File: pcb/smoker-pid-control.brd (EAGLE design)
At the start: 90 x 60 mm, 12 parts, among them SW1 EC12E_SW

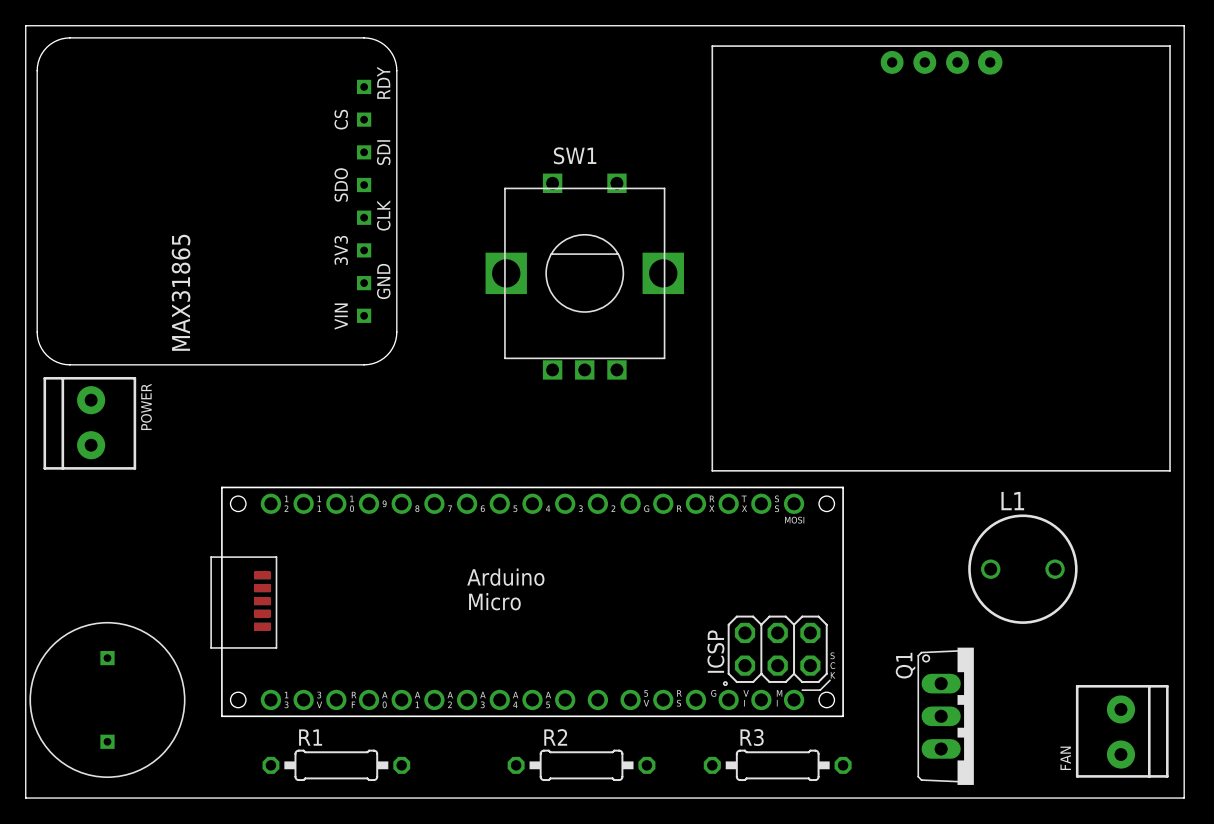
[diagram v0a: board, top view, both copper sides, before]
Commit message: pcb with pulldown on gate
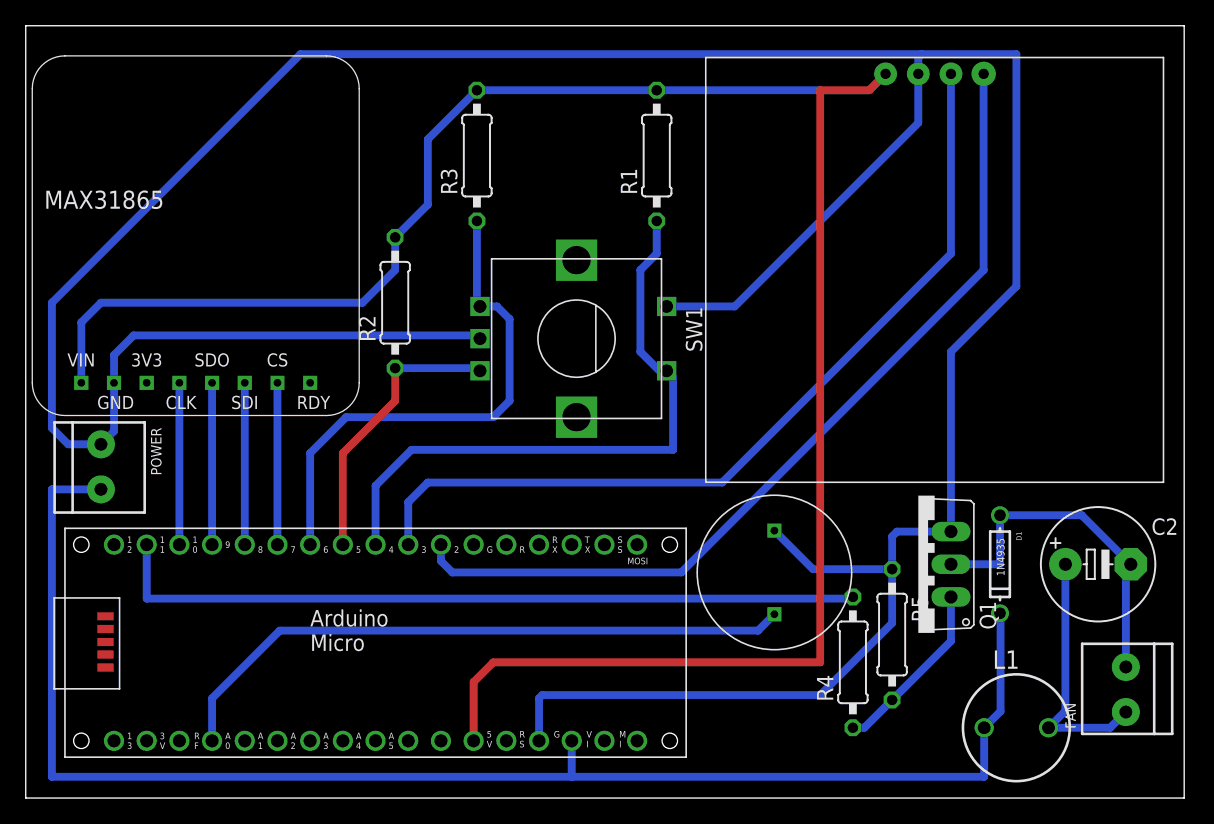
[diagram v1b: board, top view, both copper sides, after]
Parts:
- added C2: 47uF, rcl:E5-8,5
- added D1: 1N4935, adafruit:DO-1N4148
- added R4: 1.2k, rcl:0207/10
- added R5: 100k, rcl:0207/10
- FAN: value (none) -> 12V Fan
- L1: value 07HCP-100U -> 47mH
- POWER: value (none) -> 12V
- Q1: value (none) -> IRLIZ44N
- moved R1 53.5 mm to (49.0, 49.9), turned to 90 degrees
- moved R3 52.8 mm to (35.1, 49.9), turned to 90 degrees
- moved U$3 52.8 mm to (58.2, 17.5)
- moved R2 38.7 mm to (28.7, 38.5), turned to 90 degrees
- moved PCB1 12.6 mm to (3.05, 3.17)
- moved Q1 12.6 mm to (69.3, 18.2), turned to 90 degrees
- moved L1 12.3 mm to (77.0, 5.46)
- moved SW1 5.11 mm to (42.8, 35.7), turned to 270 degrees
- moved POWER 3.51 mm to (5.84, 25.8)
- moved FAN 3.32 mm to (85.5, 8.38)
- moved U$1 3.14 mm to (13.2, 43.7), turned to 0 degrees
- moved U$2 1.02 mm to (66.8, 56.3)
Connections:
- new net N$11: C2.+, FAN.2, L1.2
- new net N$12: Q1.1, R4.1, R5.2
- new net N$14: C2.-, D1.A, FAN.1, Q1.2
- new net PWM: PCB1.D11, R4.2
- net +12V: now also D1.C, L1.1
- net GND: now also Q1.3, R5.1
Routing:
- net GND: track 0.00 -> 258.6 mm
- net +5V: track 0.00 -> 161.8 mm
- net +12V: track 0.00 -> 114.6 mm
- net N$1: track 0.00 -> 68.8 mm
- net N$2: track 0.00 -> 67.4 mm
- net PWM: track 0.00 -> 59.1 mm
- net N$10: track 0.00 -> 49.7 mm
- net N$4: track 0.00 -> 48.7 mm
- net N$9: track 0.00 -> 40.1 mm
- net N$14: track 0.00 -> 27.5 mm
- net N$8: track 0.00 -> 22.1 mm
- net N$11: track 0.00 -> 19.8 mm
- net N$12: track 0.00 -> 13.8 mm
- net N$7: track 0.00 -> 12.6 mm
- net N$6: track 0.00 -> 12.6 mm
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
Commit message: fix drill hole sizes, fix oled wiring bug
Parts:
- R2: device rcl:0207/10 -> rcl:0207/15
- moved R3 0.13 mm to (35.1, 50.0)
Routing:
- net GND: track 258.6 -> 278.1 mm
- net N$9: track 40.1 -> 36.0 mm
- net N$8: track 22.1 -> 20.2 mm
- net PWM: track 59.1 -> 57.6 mm
- net N$4: track 48.7 -> 47.8 mm
- net +5V: track 161.8 -> 162.6 mm

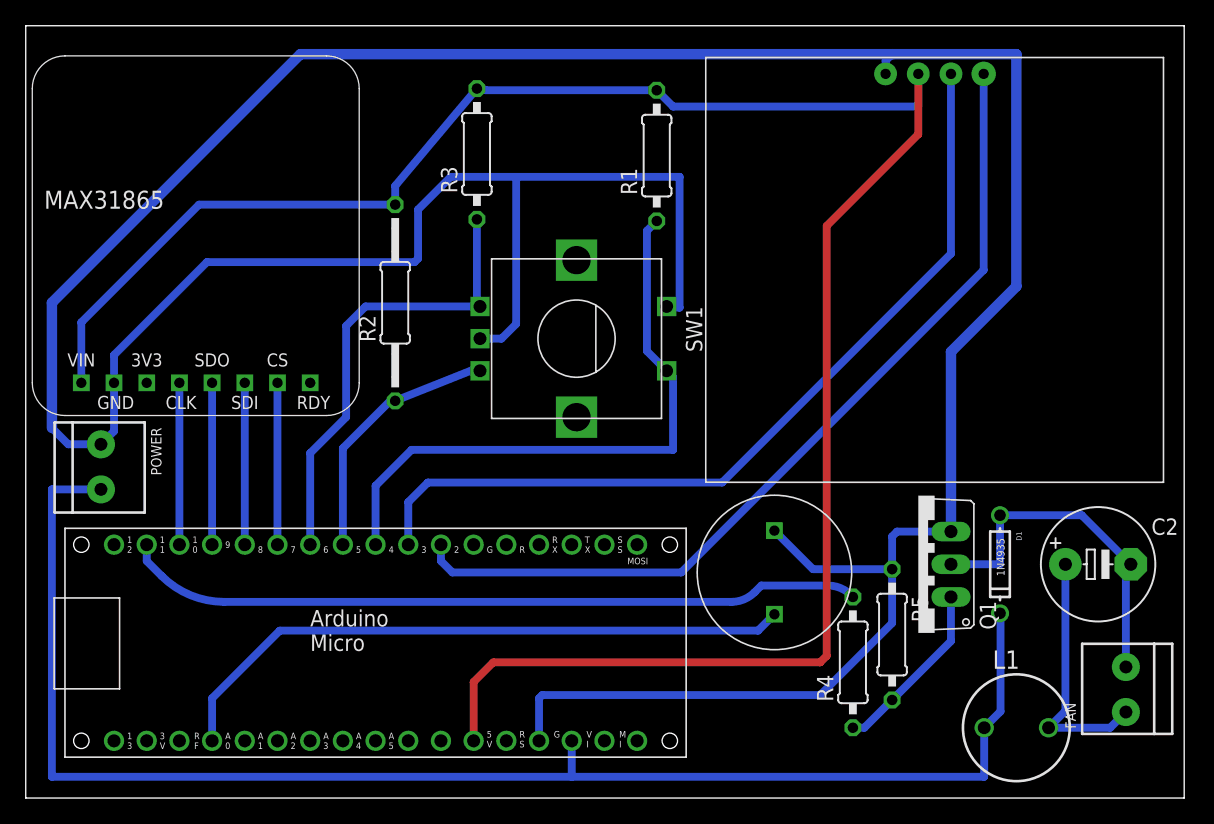
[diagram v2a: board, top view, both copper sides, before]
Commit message: single layer Layout, groundplane fix, stronger airwires
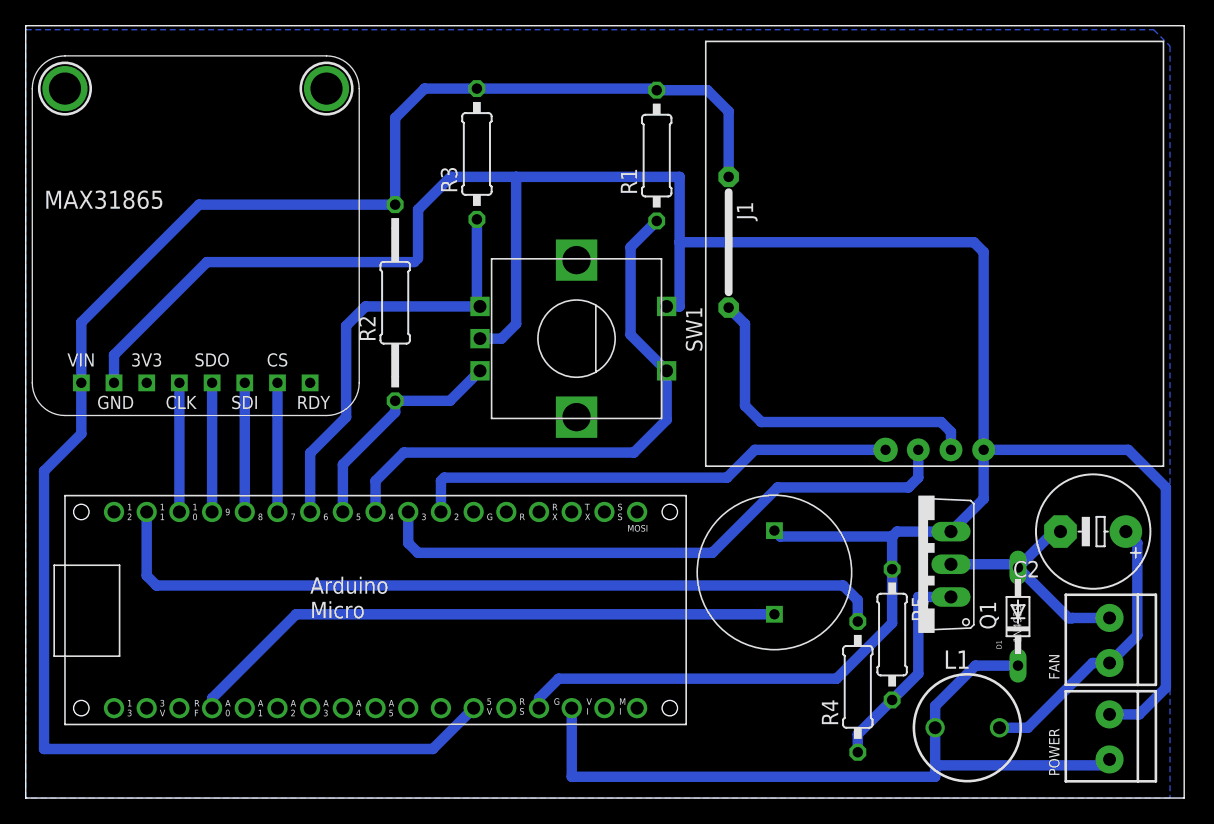
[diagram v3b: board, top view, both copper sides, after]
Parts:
- added J1: J10MM, jumper:10
- D1: device adafruit:DO-1N4148 -> diode:DO34-7
- moved POWER 81.1 mm to (84.2, 4.70), turned to 90 degrees
- moved U$2 30.2 mm to (74.4, 27.1), turned to 180 degrees
- moved D1 4.30 mm to (77.1, 14.1), turned to 90 degrees
- moved FAN 4.02 mm to (84.2, 12.2)
- moved L1 3.81 mm to (73.2, 5.46)
- moved C2 2.57 mm to (82.9, 20.7), turned to 180 degrees
- moved PCB1 2.54 mm to (3.05, 5.71)
- moved R4 1.94 mm to (64.6, 8.64)
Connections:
- new net N$13: J1.2, U$2.VCC
- net +12V: now also POWER.2; no longer POWER.1
- net +5V: now also J1.1; no longer U$2.VCC
- net GND: now also POWER.1; no longer POWER.2
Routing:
- net GND: track 278.1 -> 214.1 mm
- net +12V: track 114.6 -> 60.5 mm
- net N$1: track 68.8 -> 38.0 mm
- net N$13: track 0.00 -> 26.4 mm
- net +5V: track 162.6 -> 136.6 mm
- net N$2: track 67.4 -> 46.9 mm
- net N$14: track 27.5 -> 18.5 mm
- net PWM: track 57.6 -> 62.6 mm
- net N$4: track 47.8 -> 44.4 mm
- net N$12: track 13.8 -> 16.6 mm
- net N$10: track 49.7 -> 47.2 mm
- net N$7: track 12.6 -> 10.0 mm
- net N$6: track 12.6 -> 10.0 mm
- net N$5: track 12.6 -> 10.0 mm
- net N$3: track 12.6 -> 10.0 mm
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- added copper zone on layer 16, net GND

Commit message: final pcb
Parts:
- moved U$2 8.13 mm to (80.8, 32.1)
- moved U$3 8.13 mm to (64.5, 22.6)
- moved POWER 8.13 mm to (90.6, 9.78)
- moved C2 8.13 mm to (89.3, 25.8)
- moved FAN 8.13 mm to (90.6, 17.3)
- moved R3 8.13 mm to (41.4, 55.1)
- moved J1 8.13 mm to (61.0, 48.3)
- moved PCB1 8.13 mm to (9.40, 10.8)
- moved R1 8.13 mm to (55.4, 55.0)
- moved SW1 8.13 mm to (49.1, 40.8)
- moved R2 8.13 mm to (35.1, 43.6)
- moved R5 8.13 mm to (73.7, 17.8)
- moved U$1 8.13 mm to (19.6, 48.8)
- moved D1 8.13 mm to (83.4, 19.2)
- moved L1 8.13 mm to (79.5, 10.5)
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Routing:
- net +5V: track 136.6 -> 132.5 mm
- net GND: track 214.1 -> 216.5 mm
- net +12V: track 60.5 -> 59.1 mm
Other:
- board size 90 x 60 mm -> 100 x 70 mm

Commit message: optimise space
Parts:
- moved SW1 2.54 mm to (46.6, 40.8)
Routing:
- net GND: track 216.5 -> 220.9 mm
- net N$8: track 17.9 -> 15.3 mm
- net N$9: track 33.5 -> 31.8 mm
- net N$4: track 44.4 -> 45.2 mm
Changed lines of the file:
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@@
 <setting verticaltext="up"/>
 </settings>
-<grid distance="50" unitdist="mil" unit="mm" style="lines" multiple="1" display="no" altdistance="5" altunitdist="mil" altunit="mil"/>
+<grid distance="50" unitdist="mil" unit="mil" style="lines" multiple="1" display="no" altdistance="5" altunitdist="mil" altunit="mil"/>
 <layers>
 <layer number="1" name="Top" color="4" fill="1" visible="yes" active="yes"/>
@@
 <element name="U$1" library="smoker-pid-control" package="MAX31865-BRD" value="ADAFRUIT-MAX31865" x="19.558" y="48.768" smashed="yes" grouprefs="G1"/>
 <element name="U$2" library="smoker-pid-control" package="1.3&quot;OLED" value="13&quot;OLED13&quot;OLED" x="80.772" y="32.131" smashed="yes" rot="R180" grouprefs="G1"/>
-<element name="SW1" library="smoker-pid-control" package="ALPS_EC12E_SW" package3d_urn="urn:adsk.eagle:package:27083/1" value="EC12E_SW" x="49.142" y="40.771" smashed="yes" rot="R270" grouprefs="G1">
-<attribute name="MF" value="" x="49.142" y="40.771" size="1.778" layer="27" rot="R270" display="off"/>
-<attribute name="MPN" value="EC12E2424407" x="49.142" y="40.771" size="1.778" layer="27" rot="R270" display="off"/>
-<attribute name="NAME" x="57.642" y="43.271" size="1.27" layer="25" rot="R270"/>
-<attribute name="OC_FARNELL" value="1520813" x="49.142" y="40.771" size="1.778" layer="27" rot="R270" display="off"/>
-<attribute name="OC_NEWARK" value="74M1068" x="49.142" y="40.771" size="1.778" layer="27" rot="R270" display="off"/>
-<attribute name="POPULARITY" value="3" x="49.142" y="40.771" size="1.778" layer="27" rot="R270" display="off"/>
-<attribute name="VALUE" x="40.142" y="37.271" size="1.27" layer="27" rot="R90"/>
+<element name="SW1" library="smoker-pid-control" package="ALPS_EC12E_SW" package3d_urn="urn:adsk.eagle:package:27083/1" value="EC12E_SW" x="46.602" y="40.771" smashed="yes" rot="R270" grouprefs="G1">
+<attribute name="MF" value="" x="46.602" y="40.771" size="1.778" layer="27" rot="R270" display="off"/>
+<attribute name="MPN" value="EC12E2424407" x="46.602" y="40.771" size="1.778" layer="27" rot="R270" display="off"/>
+<attribute name="NAME" x="55.102" y="43.271" size="1.27" layer="25" rot="R270"/>
+<attribute name="OC_FARNELL" value="1520813" x="46.602" y="40.771" size="1.778" layer="27" rot="R270" display="off"/>
+<attribute name="OC_NEWARK" value="74M1068" x="46.602" y="40.771" size="1.778" layer="27" rot="R270" display="off"/>
+<attribute name="POPULARITY" value="3" x="46.602" y="40.771" size="1.778" layer="27" rot="R270" display="off"/>
+<attribute name="VALUE" x="37.602" y="37.271" size="1.27" layer="27" rot="R90"/>
 </element>
 <element name="POWER" library="smoker-pid-control" package="TERMBLOCK_1X2-3.5MM" value="12V" x="90.551" y="9.779" smashed="yes" rot="R90" grouprefs="G1">
@@
 <wire x1="73.66" y1="22.86" x2="73.66" y2="18.669" width="0.8128" layer="16"/>
 <wire x1="73.66" y1="18.669" x2="69.342" y2="14.351" width="0.8128" layer="16"/>
-<wire x1="41.642" y1="40.771" x2="43.311" y2="40.771" width="0.8128" layer="16"/>
-<wire x1="43.311" y1="40.771" x2="44.45" y2="41.91" width="0.8128" layer="16"/>
-<wire x1="44.45" y1="41.91" x2="44.45" y2="53.34" width="0.8128" layer="16"/>
-<wire x1="44.45" y1="53.34" x2="39.37" y2="53.34" width="0.8128" layer="16"/>
+<wire x1="39.102" y1="40.771" x2="43.18" y2="40.771" width="0.8128" layer="16"/>
+<wire x1="43.18" y1="40.771" x2="43.18" y2="53.34" width="0.8128" layer="16"/>
+<wire x1="43.18" y1="53.34" x2="39.37" y2="53.34" width="0.8128" layer="16"/>
 <wire x1="36.83" y1="50.8" x2="36.83" y2="46.99" width="0.8128" layer="16"/>
 <wire x1="36.83" y1="46.99" x2="36.556715625" y2="46.716715625" width="0.6096" layer="16"/>
 <wire x1="36.556715625" y1="46.716715625" x2="20.427715625" y2="46.716715625" width="0.8128" layer="16"/>
 <wire x1="39.37" y1="53.34" x2="36.83" y2="50.8" width="0.8128" layer="16"/>
-<wire x1="57.15" y1="43.271" x2="56.142" y2="43.271" width="0.8128" layer="16"/>
+<wire x1="57.15" y1="43.271" x2="53.602" y2="43.271" width="0.8128" layer="16"/>
 <wire x1="57.15" y1="48.26" x2="57.15" y2="43.271" width="0.8128" layer="16"/>
 <wire x1="64.516" y1="25.856" x2="64.972" y2="25.4" width="0.8128" layer="16"/>
@@
 </polygon>
 <wire x1="58.42" y1="48.26" x2="57.15" y2="48.26" width="0.8128" layer="16"/>
-<wire x1="44.45" y1="53.34" x2="45.72" y2="54.61" width="0.8128" layer="16"/>
-<wire x1="45.72" y1="54.61" x2="57.15" y2="54.61" width="0.8128" layer="16"/>
+<wire x1="43.18" y1="53.34" x2="44.45" y2="54.61" width="0.8128" layer="16"/>
+<wire x1="44.45" y1="54.61" x2="57.15" y2="54.61" width="0.8128" layer="16"/>
 <wire x1="57.15" y1="54.61" x2="58.42" y2="53.34" width="0.8128" layer="16"/>
 <wire x1="58.42" y1="53.34" x2="58.42" y2="48.26" width="0.8128" layer="16"/>
@@
 <contactref element="SW1" pad="E"/>
 <contactref element="PCB1" pad="D4"/>
-<wire x1="53.34" y1="47.879" x2="55.372" y2="49.911" width="0.8128" layer="16"/>
-<wire x1="53.34" y1="41.073" x2="53.34" y2="47.879" width="0.8128" layer="16"/>
+<wire x1="54.102" y1="49.911" x2="55.372" y2="49.911" width="0.8128" layer="16"/>
+<wire x1="54.102" y1="49.911" x2="50.8" y2="46.609" width="0.8128" layer="16"/>
+<wire x1="50.8" y1="41.073" x2="50.8" y2="46.609" width="0.8128" layer="16"/>
 <wire x1="53.602" y1="31.921" x2="35.731" y2="31.921" width="0.8128" layer="16"/>
-<wire x1="56.142" y1="34.461" x2="53.602" y2="31.921" width="0.8128" layer="16"/>
-<wire x1="56.142" y1="34.461" x2="56.142" y2="38.271" width="0.8128" layer="16"/>
+<wire x1="53.602" y1="31.921" x2="53.602" y2="38.271" width="0.8128" layer="16"/>
 <wire x1="33.528" y1="27.305" x2="33.528" y2="29.718" width="0.8128" layer="16"/>
 <wire x1="35.731" y1="31.921" x2="33.528" y2="29.718" width="0.8128" layer="16"/>
-<wire x1="56.142" y1="38.271" x2="53.34" y2="41.073" width="0.8128" layer="16"/>
+<wire x1="53.602" y1="38.271" x2="50.8" y2="41.073" width="0.8128" layer="16"/>
 </signal>
 <signal name="N$8">
@@
 <wire x1="30.988" y1="30.988" x2="35.052" y2="35.052" width="0.8128" layer="16"/>
 <wire x1="35.052" y1="35.052" x2="35.052" y2="35.941" width="0.8128" layer="16"/>
-<wire x1="35.052" y1="35.941" x2="39.312" y2="35.941" width="0.8128" layer="16"/>
-<wire x1="39.312" y1="35.941" x2="41.642" y2="38.271" width="0.8128" layer="16"/>
+<wire x1="35.052" y1="35.941" x2="36.772" y2="35.941" width="0.8128" layer="16"/>
+<wire x1="36.772" y1="35.941" x2="39.102" y2="38.271" width="0.8128" layer="16"/>
 </signal>
 <signal name="N$9">
@@
 <contactref element="SW1" pad="A"/>
 <contactref element="PCB1" pad="D6"/>
-<wire x1="41.642" y1="43.271" x2="32.752" y2="43.271" width="0.8128" layer="16"/>
+<wire x1="39.102" y1="43.271" x2="32.752" y2="43.271" width="0.8128" layer="16"/>
 <wire x1="32.752" y1="43.271" x2="31.242" y2="41.761" width="0.8128" layer="16"/>
 <wire x1="31.242" y1="34.671" x2="31.242" y2="41.761" width="0.8128" layer="16" grouprefs="G1"/>
 <wire x1="28.448" y1="31.877" x2="28.448" y2="27.305" width="0.8128" layer="16" grouprefs="G1"/>
 <wire x1="31.242" y1="34.671" x2="28.448" y2="31.877" width="0.8128" layer="16" grouprefs="G1"/>
-<wire x1="41.402" y1="50.038" x2="41.402" y2="43.511" width="0.8128" layer="16"/>
-<wire x1="41.402" y1="43.511" x2="41.642" y2="43.271" width="0.6096" layer="16"/>
+<wire x1="41.402" y1="50.038" x2="40.132" y2="48.768" width="0.8128" layer="16"/>
+<wire x1="40.132" y1="48.768" x2="40.132" y2="44.301" width="0.8128" layer="16"/>
+<wire x1="40.132" y1="44.301" x2="39.102" y2="43.271" width="0.8128" layer="16"/>
 </signal>
 <signal name="N$10">
